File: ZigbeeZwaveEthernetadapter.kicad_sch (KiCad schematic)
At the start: 16 parts, among them J1 Barrel_Jack, J11 Conn_02x06_Odd_Even, J12 Conn_01x06, J14 Conn_01x06, J2 USB_B_Micro, J21 Conn_02x06_Odd_Even, J22 Conn_01x06, J24 Conn_01x06, J3 USB4125-GF-A, J31 Conn_02x05_Odd_Even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

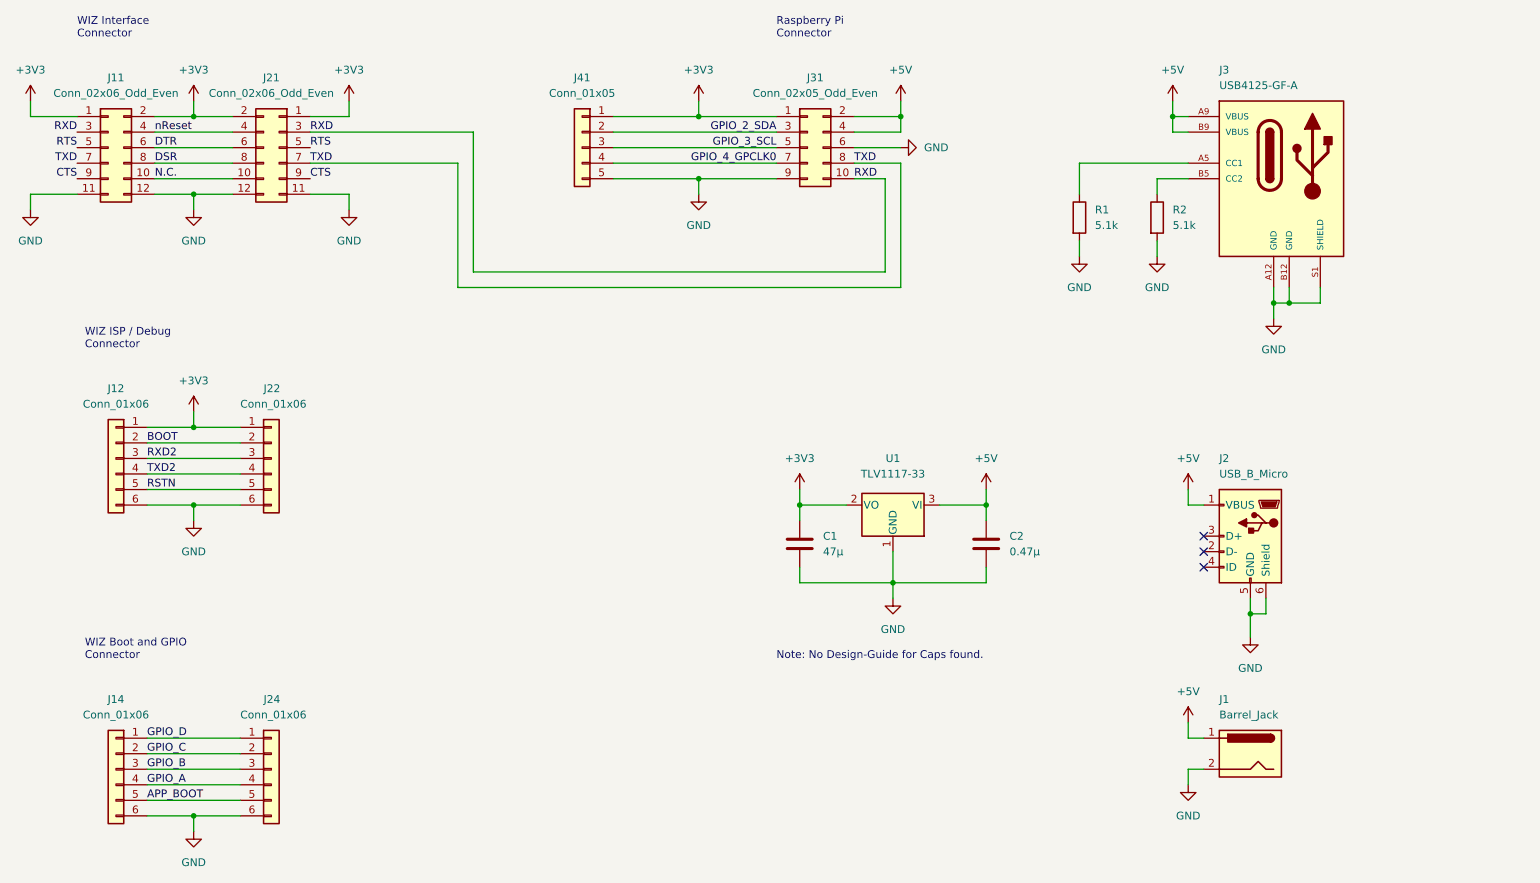
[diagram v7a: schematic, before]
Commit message: Add: Solder bridges and RX and TX LEDs
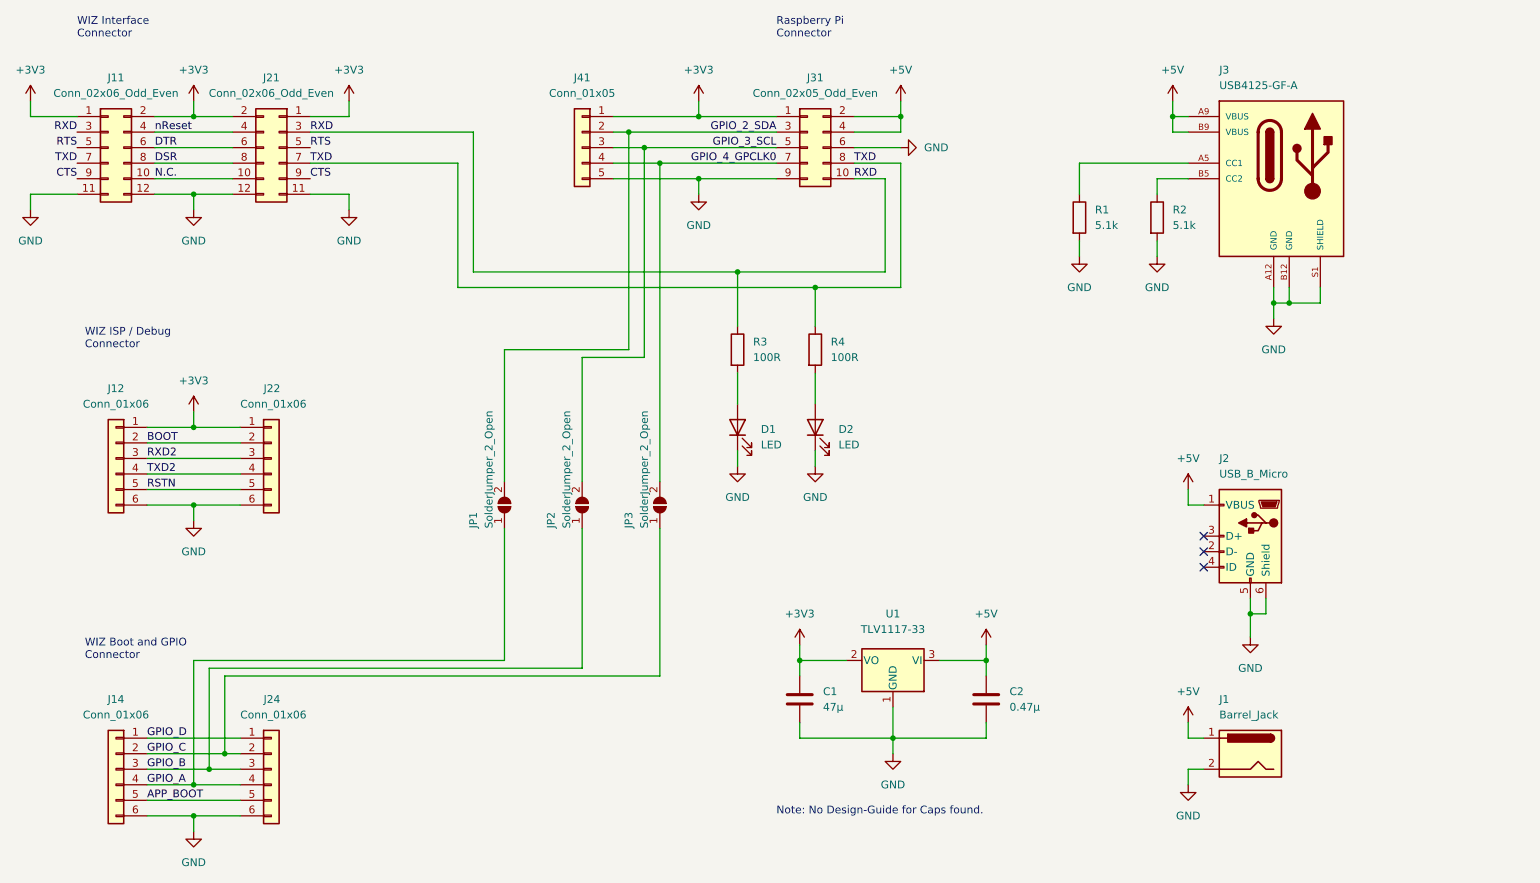
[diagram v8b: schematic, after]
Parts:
- added D1, D2: LED, LED_SMD:LED_0805_2012Metric_Pad1.15x1.40mm_HandSolder, symbol Device:LED
- added JP1, JP2, JP3: SolderJumper_2_Open, Jumper:SolderJumper-2_P1.3mm_Open_TrianglePad1.0x1.5mm, symbol Jumper:SolderJumper_2_Open
- added R3, R4: 100R, Resistor_SMD:R_0805_2012Metric_Pad1.20x1.40mm_HandSolder, symbol Device:R
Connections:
- net GND: now also D1.1 (K), D2.1 (K)
- net GPIO_2_SDA: now also JP1.2 (B)
- net GPIO_3_SCL: now also JP2.2 (B)
- net GPIO_4_GPCLK0: now also JP3.2 (B)
- net GPIO_A: now also JP1.1 (A)
- net GPIO_B: now also JP2.1 (A)
- net GPIO_C: now also JP3.1 (A)
- net RXD: now also R3.1
- net TXD: now also R4.1
- new net: D2.2 (A), R4.2
- new net: D1.2 (A), R3.2
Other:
- moved on the sheet: C1, C2, U1
